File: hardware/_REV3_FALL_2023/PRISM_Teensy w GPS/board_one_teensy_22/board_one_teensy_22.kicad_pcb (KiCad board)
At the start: 2 copper layers, 61 x 88.9 mm, 27 parts, among them J1 Micro_SD_Card_Det_Hirose_DM3AT, J3 3387, U1 Teensy4.0, U2 GPS-14414, U3 3966, U4 RFM69HCW_Breakout, U5 SFN-1407PA7.6

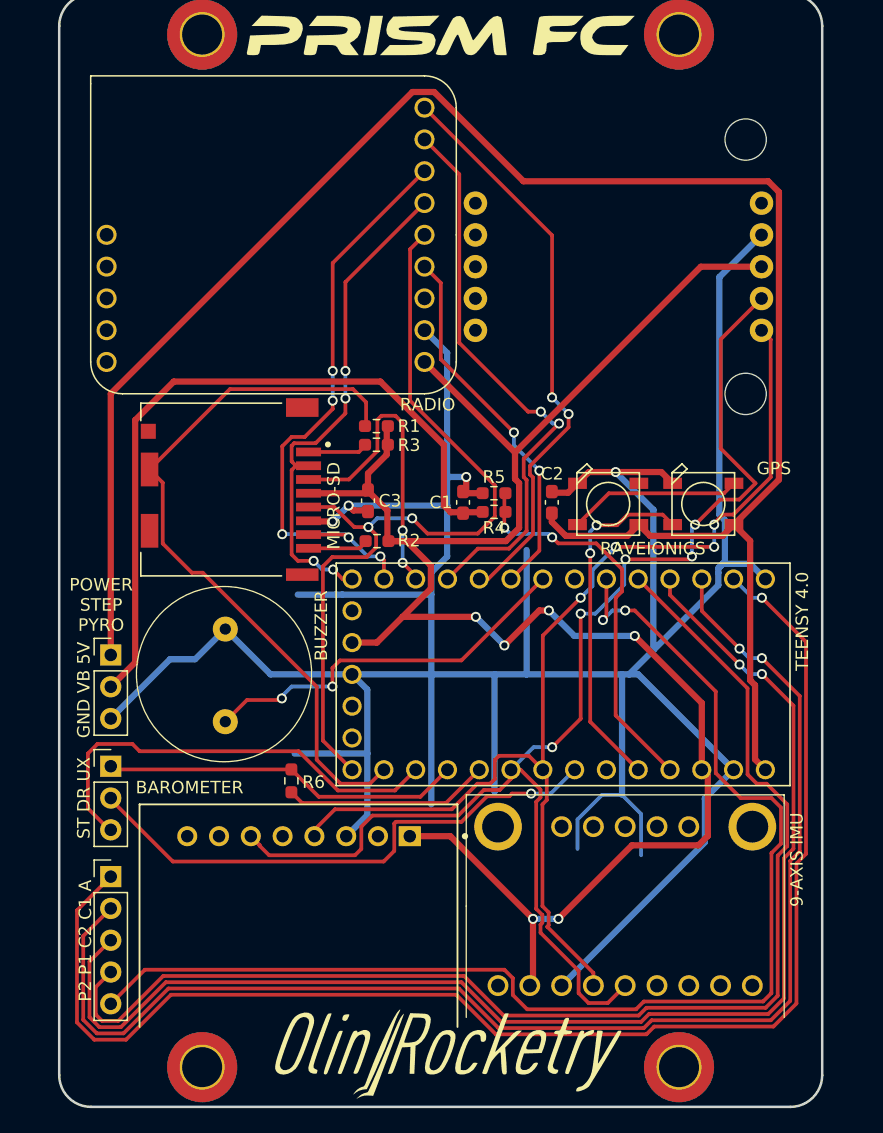
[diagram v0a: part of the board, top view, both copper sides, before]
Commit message: Add grounded mount on FC
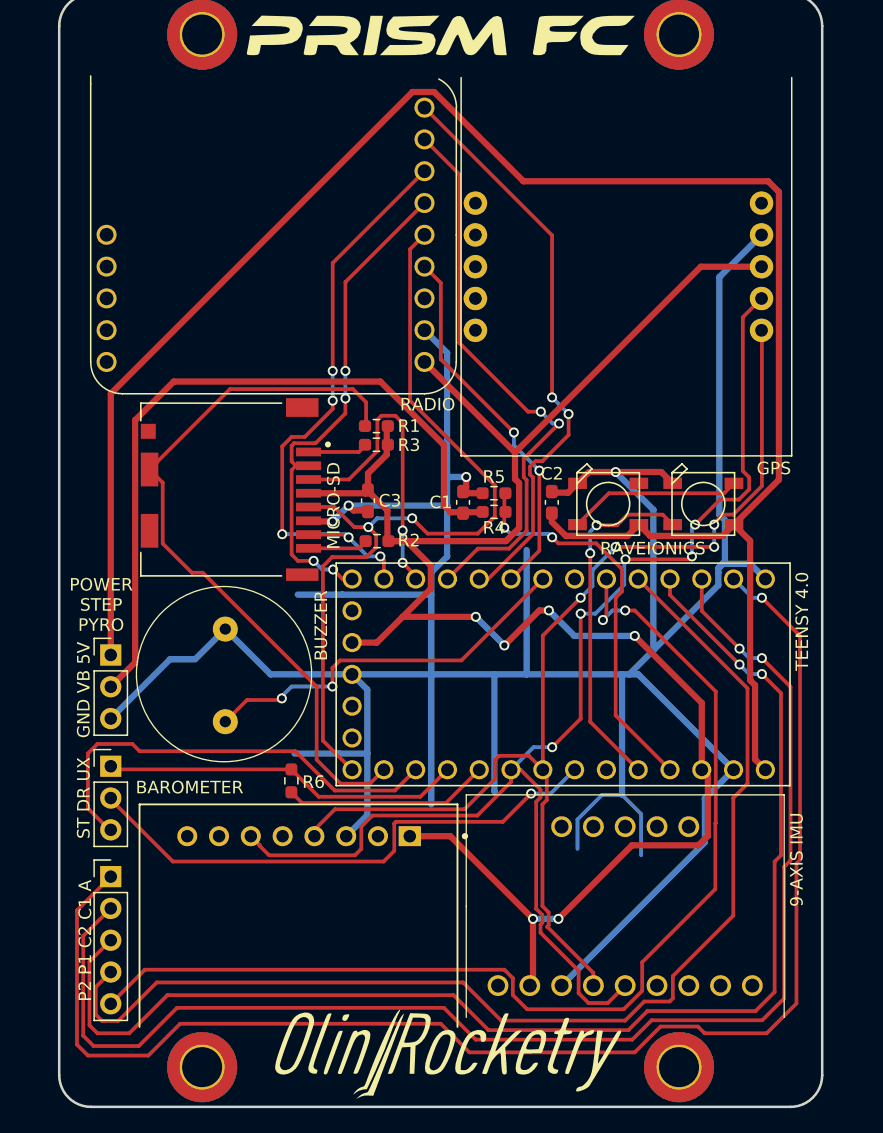
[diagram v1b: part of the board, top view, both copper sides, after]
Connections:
- H4 pad 1: (no net) -> GND
- U1 pad 5: /EN -> unconnected-(U1-Pad5)
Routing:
- net /PYRO 2: track 100.0 -> 88.0 mm
- net /PYRO 1: track 101.0 -> 93.1 mm
- net /SDA: track 105.0 -> 103.2 mm
- net /ARM: track 111.7 -> 113.1 mm
- net /CONT 2: track 104.7 -> 103.7 mm
- net /SCL: track 89.9 -> 89.3 mm
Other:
- board text added: "Alex Mineeva"
- board text added: "Ari Bobesh"
- board text added: "DESIGN BY"
- board text added: "Daniel Theunissen"
- board text added: "Ertug Umsur"
- board text added: "Ishan Porwal"
- board text added: "Joseph Liu"
- board text added: "Mateo Brancoli"
- board text added: "Nividh Singh"
- board text added: "Rohan Shah"
- board text added: "Rowan Jansens"

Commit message: Update board_one_teensy_22.kicad_pcb
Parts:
- removed the ? at (138.1, 134.5)
- added G***: LOGO, LOGO, F.Cu at (138.1, 135.6)

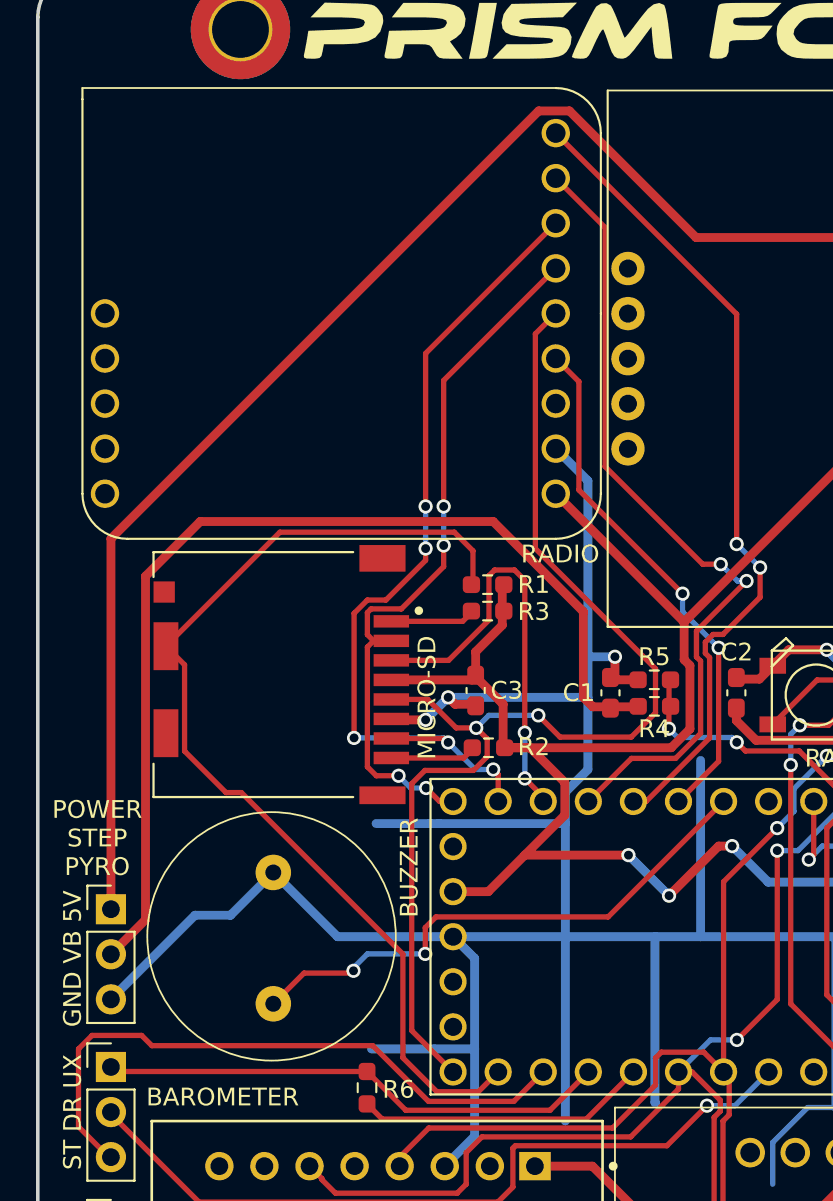
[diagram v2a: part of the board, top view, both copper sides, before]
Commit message: Add big buzzer to FC
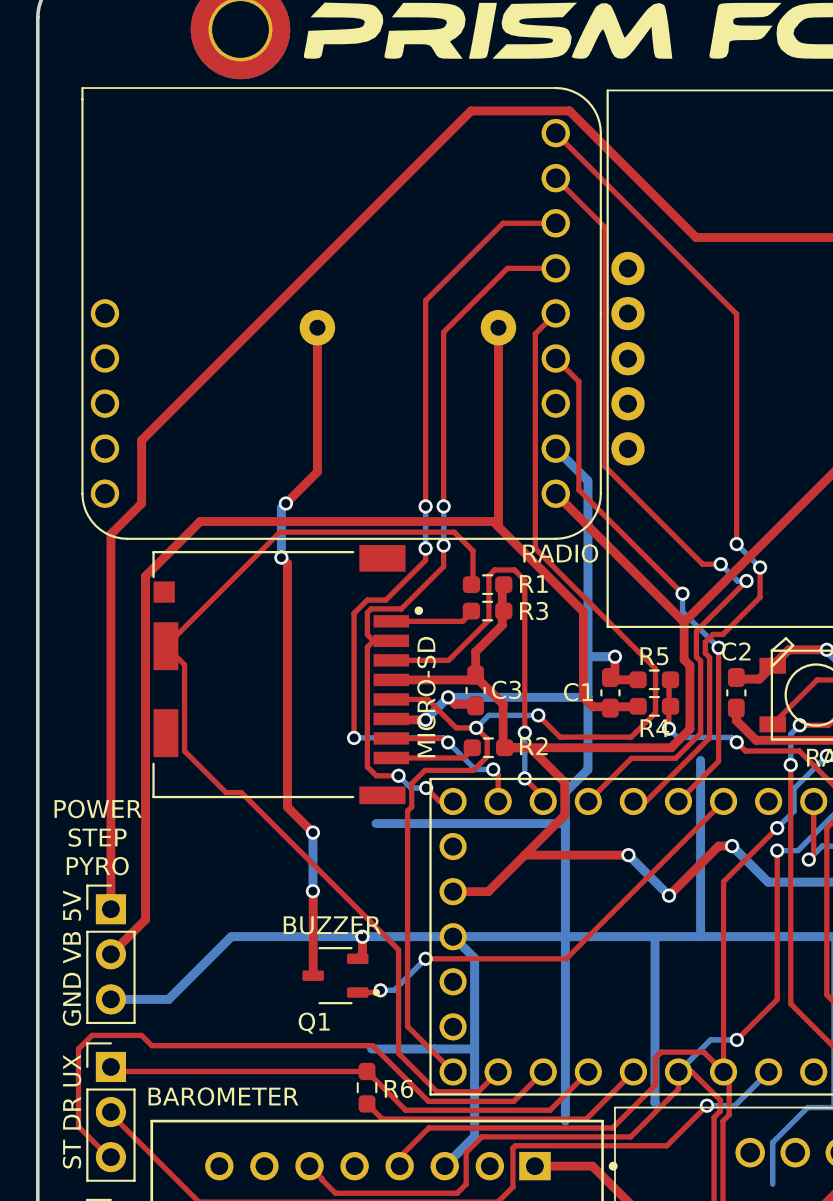
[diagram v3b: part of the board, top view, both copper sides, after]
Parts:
- added Q1: AO3400A, rocketry_footprints:SOT95P280X125-3N, F.Cu at (124.0, 106.6)
- U5: value SFN-1407PA7.6 -> CT25E-16T150-1; footprint rocketry_footprints:SFN-1407PA7.6 -> rocketry_footprints:CT25E-16T150-1; moved to B.Cu
- moved U5 35.1 mm to (128.0, 70.1), turned to 180 degrees
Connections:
- U5 pad 1: /BUZZER -> /VBAT
- U5 pad 2: GND -> Net-(U5-N)
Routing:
- net Net-(U5-N): track 0.00 -> 38.1 mm, vias 0 -> 4
- net /VBAT: track 58.4 -> 69.6 mm
- net /BUZZER: track 31.1 -> 25.1 mm
- net /5V: track 153.2 -> 155.4 mm
- net /MOSI: track 48.1 -> 49.9 mm
- net GND: track 279.3 -> 277.6 mm, vias 4 -> 5
- net /MISO: track 40.4 -> 42.0 mm

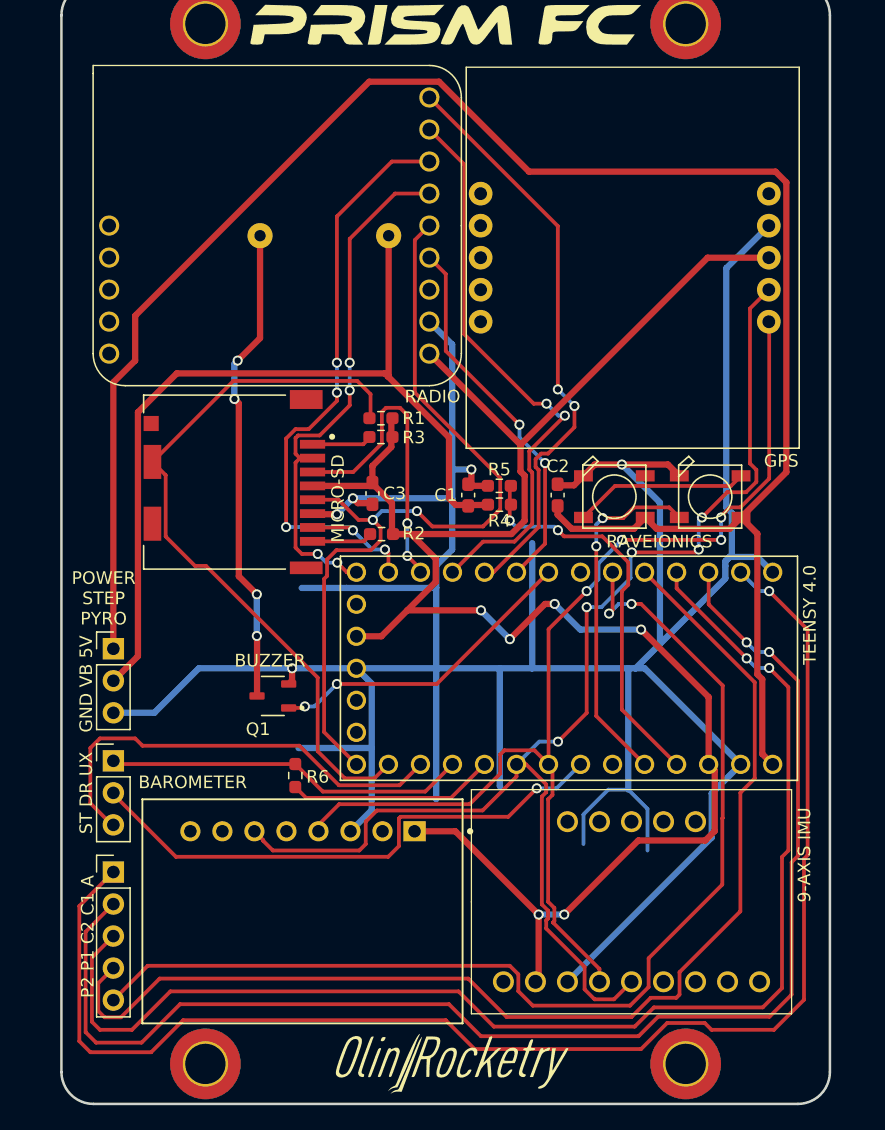
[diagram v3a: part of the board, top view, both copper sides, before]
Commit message: Add two buzzers to FC
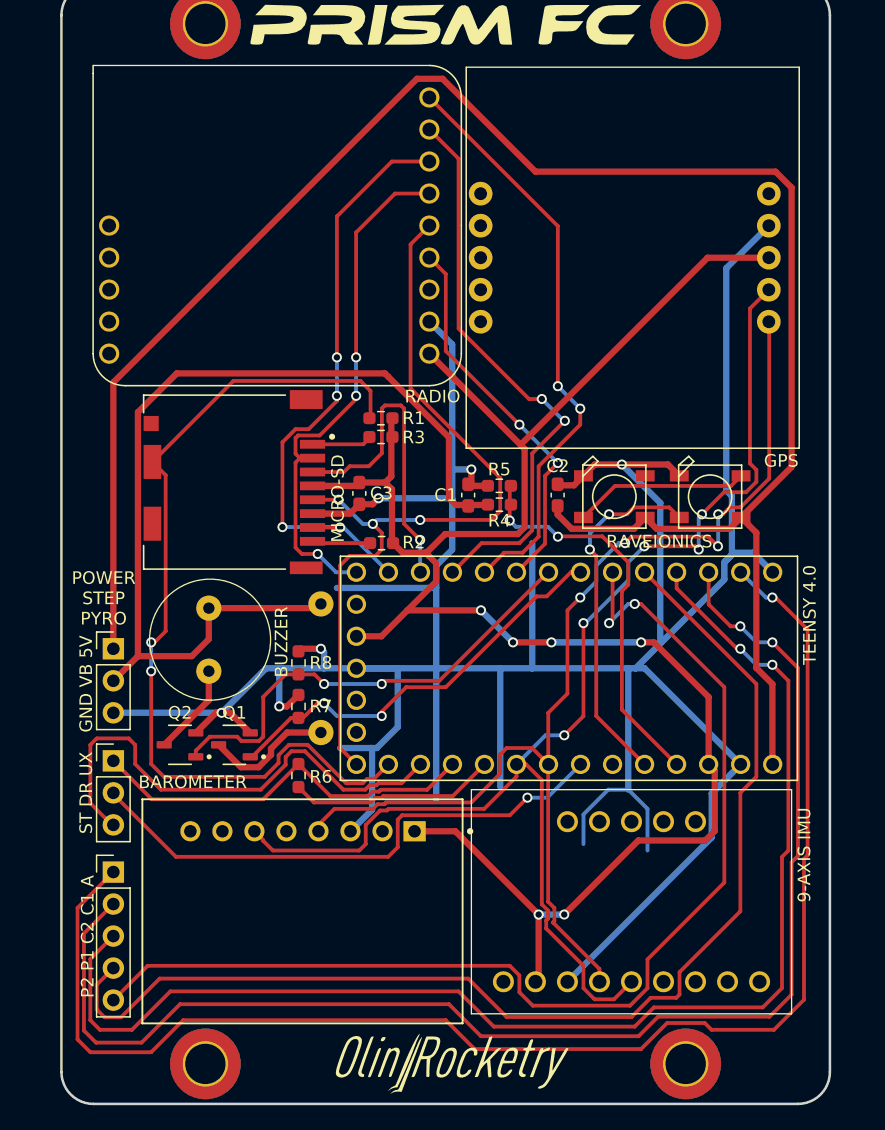
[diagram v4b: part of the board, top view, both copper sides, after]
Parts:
- added Q2: AO3400A, rocketry_footprints:SOT95P280X125-3N, F.Cu at (116.6, 110.5)
- added R7: 10k, Resistor_SMD:R_0603_1608Metric_Pad0.98x0.95mm_HandSolder, F.Cu at (126.0, 107.4)
- added R8: 10k, Resistor_SMD:R_0603_1608Metric_Pad0.98x0.95mm_HandSolder, F.Cu at (126.0, 104.0)
- added U6: CMI-9605-1280T, rocketry_footprints:CMI-9605-1280T, F.Cu at (118.9, 102.1)
- moved U5 34.3 mm to (127.8, 104.4), turned to -90 degrees
- moved Q1 4.93 mm to (120.9, 110.5)
- moved C3 1.04 mm to (130.8, 90.5)
- moved R2 0.72 mm to (132.6, 94.5)
- moved R6 0.25 mm to (126.0, 112.9)
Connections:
- Q1 pad 1: /BUZZER -> /BUZZER 1
- U1 pad 5: unconnected-(U1-Pad5) -> /BUZZER 1
- U1 pad 6: /BUZZER -> /BUZZER 2
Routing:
- net /BUZZER 2: track 0.00 -> 37.1 mm, vias 0 -> 2
- net /BUZZER 1: track 0.00 -> 33.3 mm, vias 0 -> 2
- net Net-(U5-N): track 38.1 -> 10.3 mm, vias 4 -> 0
- net /BUZZER: track 25.1 -> 0.00 mm, vias 2 -> 0
- net /SD_DETECT: track 58.2 -> 70.0 mm, vias 0 -> 2
- net GND: track 277.6 -> 286.7 mm, vias 5 -> 6
- net Net-(U6-N): track 0.00 -> 7.31 mm
- net /VBAT: track 69.6 -> 76.1 mm
- net /STEP: track 35.7 -> 39.9 mm
- net /3.3V: track 157.3 -> 153.6 mm
- net /UART: track 28.8 -> 31.4 mm
- net /SD_SCK: track 66.9 -> 64.8 mm, vias 2 -> 3
- net /MOSI: track 49.9 -> 48.3 mm, vias 5 -> 4
- net /5V: track 155.4 -> 153.8 mm
- net /SD_CS: track 24.2 -> 25.4 mm, vias 2 -> 1
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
